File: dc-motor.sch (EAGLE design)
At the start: 80 parts, among them IC1 MEGA32-A, X10 JUMP1-4, X11 JUMP1-4, X3 RIA_3POL, X4 RIA_3POL, X5 RIA_2POL, X6 JUMP1-4, X7 PFVERB10, X8 PFVERB10, X9 JUMP1-4

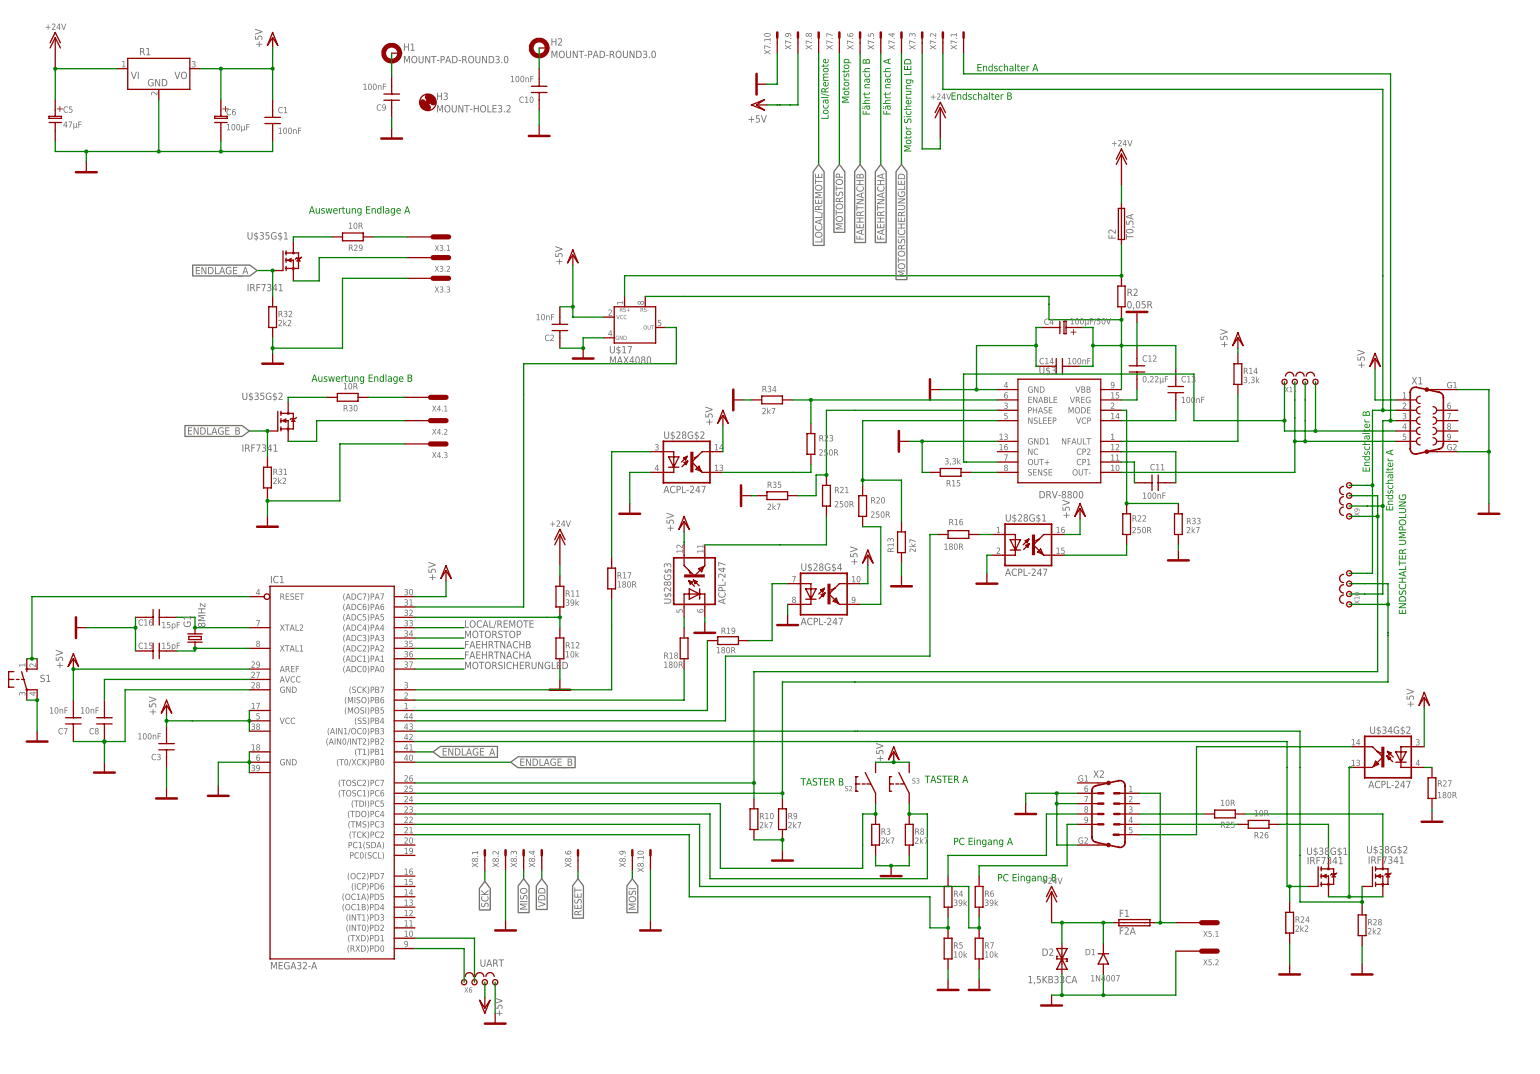
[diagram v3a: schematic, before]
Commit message: ADC wiring changed.
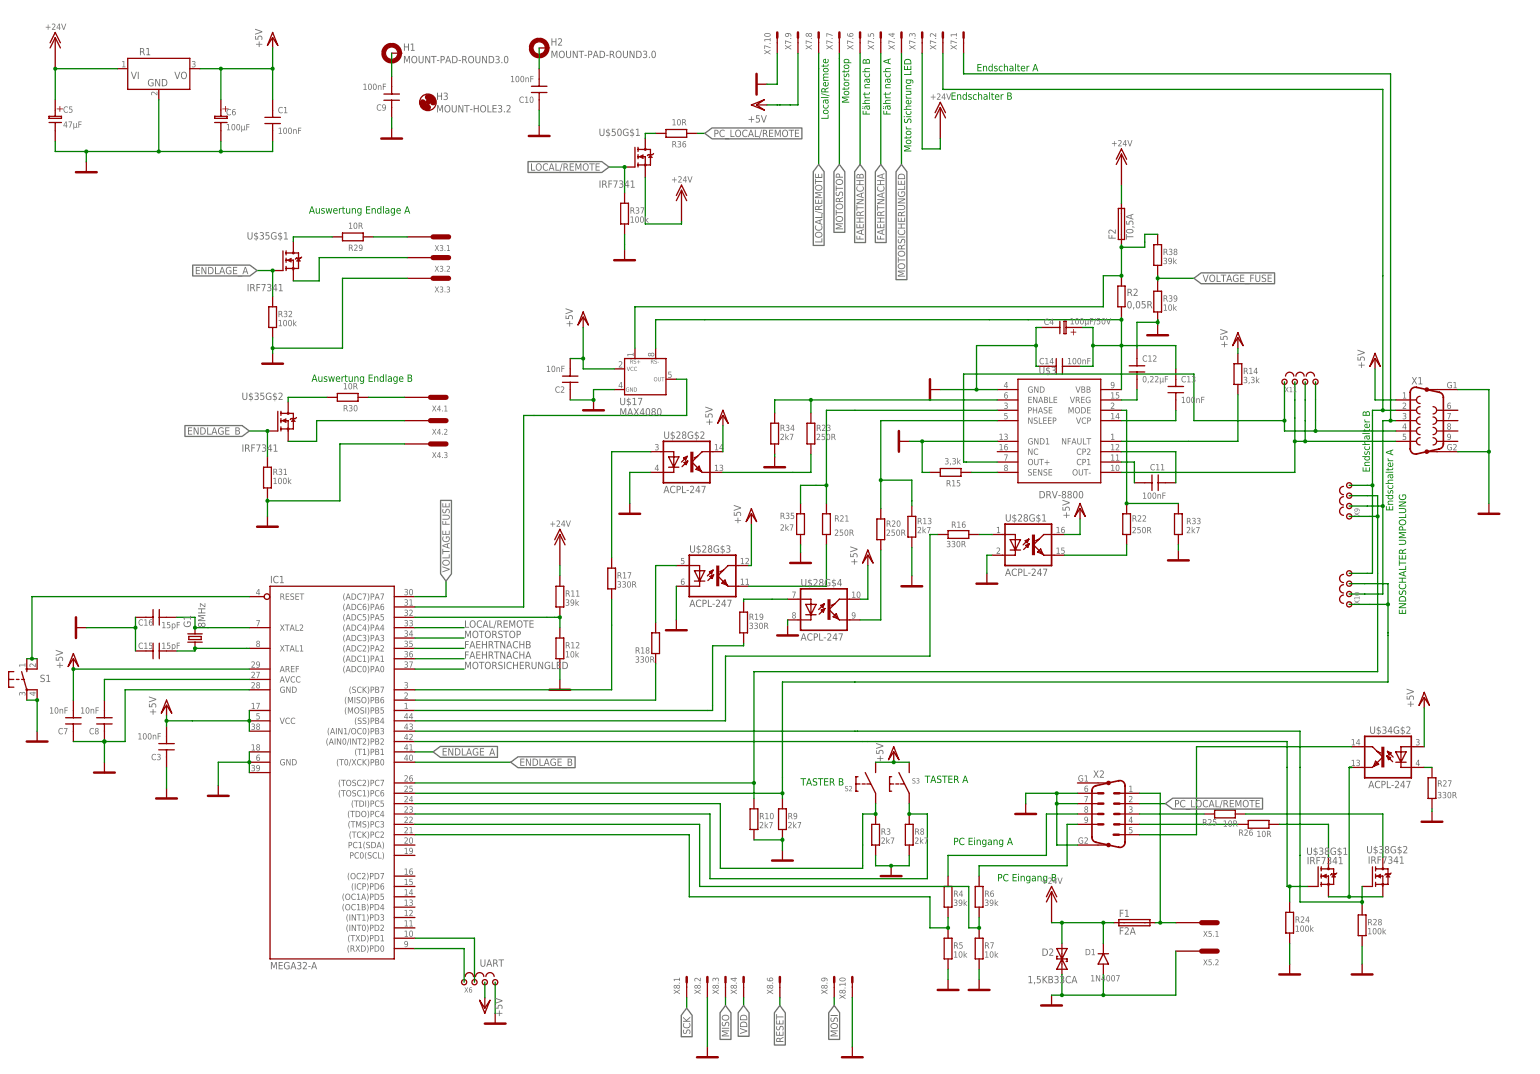
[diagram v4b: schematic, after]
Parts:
- added R36: 10R, Resistor:0805
- added R37: 100k, Resistor:0805
- added R38: 39k, Resistor:0805
- added R39: 10k, Resistor:0805
- added U$50: IRF7341, Transistor:IRF7341
- R16, R17, R18, R19, R27: value 180R -> 330R
- R24, R28, R31, R32: value 2k2 -> 100k
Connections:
- new net N$39: R36.2
- new net PC_LOCAL/REMOTE: R36.1, X2.2
- new net VOLTAGE_FUSE: IC1.(ADC7)PA7, R38.1, R39.2
- net +24V: now also U$50G$1.N-S1
- net GND: now also R37.2, R39.1
- net LOCAL/REMOTE: now also R37.1, U$50G$1.N-G1
- net N$6: now also R38.2
- net VDD: no longer IC1.(ADC7)PA7
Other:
- moved on the sheet: C2, R13, R18, R19, R20, R21, R23, R34, R35, U$17, U$28G$3, U$28G$4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

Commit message: Layout finished
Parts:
- removed X10, X11, X9: JUMP1-4, Connector:JUMP1-4
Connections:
- removed net N$30: U$3.OUT-, X1.5, X11.2, X11.3
- removed net N$5: U$3.OUT+, X1.4, X11.1, X11.4
- new net +24V_LED_µC: IC1.PC1(SDA), X7.3.1
- new net MOTOR: IC1.(INT1)PD3, X1.6
- new net N$41: U$3.OUT+, X1.4
- new net N$44: U$3.OUT-, X1.5
- new net RICHTUNG: IC1.(INT0)PD2, X1.9
- net +24V: no longer X7.3.1
- net GND: now also X1.7, X1.8, X2.G1
- net N$18: no longer X10.1, X10.3
- net N$20: no longer X10.4, X9.4
- net N$22: no longer X10.2, X9.2
- net N$25: no longer X9.1, X9.3
- net N$39: now also U$50G$1.D1
- net N$60: now also IC1.AREF; no longer IC1.AVCC
- net VDD: now also IC1.AVCC; no longer IC1.AREF
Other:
- note removed: "ENDSCHALTER UMPOLUNG"
- moved on the sheet: C7, C8, R36, R37, U$50G$1, X1

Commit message: layout checked
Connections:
- net MOTORSICHERUNGLED renamed FEHLER_LED
- removed net N$20: X1.2, X7.2.1
- removed net N$22: X1.3, X7.1.1
- net N$18: now also X1.3, X7.1.1
- net N$25: now also X1.2, X7.2.1
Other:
- note added: "Fehler_LED"
- note removed: "Motor Sicherung LED"
- moved on the sheet: R24
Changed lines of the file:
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@@
 <setting verticaltext="up"/>
 </settings>
-<grid distance="0.635" unitdist="mm" unit="mm" style="lines" multiple="1" display="yes" altdistance="0.3175" altunitdist="mm" altunit="mm"/>
+<grid distance="0.635" unitdist="mm" unit="mm" style="dots" multiple="1" display="yes" altdistance="0.3175" altunitdist="mm" altunit="mm"/>
 <layers>
 <layer number="1" name="Top" color="4" fill="1" visible="no" active="no"/>
@@
 <text x="220.98" y="259.08" size="1.778" layer="91" font="vector" rot="R270">Fährt nach A</text>
 <text x="215.9" y="259.08" size="1.778" layer="91" font="vector" rot="R270">Fährt nach B</text>
-<text x="226.06" y="259.08" size="1.778" layer="91" font="vector" rot="R270">Motor Sicherung LED</text>
+<text x="226.06" y="259.08" size="1.778" layer="91" font="vector" rot="R270">Fehler_LED</text>
 <text x="340.36" y="144.78" size="1.778" layer="91" font="vector" rot="R90">Endschalter B</text>
 <text x="345.44" y="137.16" size="1.778" layer="91" font="vector" rot="R90">Endschalter A</text>
@@
 </instance>
 <instance part="U$39" gate="G$1" x="338.455" y="34.29" smashed="yes" rot="MR0"/>
-<instance part="U$40" gate="G$1" x="320.675" y="34.29" smashed="yes" rot="MR0"/>
-<instance part="R24" gate="G$1" x="320.675" y="46.99" smashed="yes" rot="R270">
-<attribute name="NAME" x="321.945" y="46.99" size="1.524" layer="95"/>
-<attribute name="VALUE" x="321.945" y="44.7675" size="1.524" layer="96"/>
+<instance part="U$40" gate="G$1" x="320.04" y="34.29" smashed="yes" rot="MR0"/>
+<instance part="R24" gate="G$1" x="320.04" y="46.99" smashed="yes" rot="R270">
+<attribute name="NAME" x="321.31" y="46.99" size="1.524" layer="95"/>
+<attribute name="VALUE" x="321.31" y="44.7675" size="1.524" layer="96"/>
 </instance>
 <instance part="R28" gate="G$1" x="338.455" y="46.355" smashed="yes" rot="R270">
@@
 <pinref part="R24" gate="G$1" pin="2"/>
 <pinref part="U$40" gate="G$1" pin="GND"/>
-<wire x1="320.675" y1="41.91" x2="320.675" y2="36.83" width="0.1524" layer="91"/>
+<wire x1="320.04" y1="41.91" x2="320.04" y2="36.83" width="0.1524" layer="91"/>
 </segment>
 <segment>
@@
 <wire x1="196.215" y1="106.045" x2="213.995" y2="106.045" width="0.1524" layer="91"/>
 <wire x1="213.995" y1="106.045" x2="343.535" y2="106.045" width="0.1524" layer="91"/>
-<wire x1="343.535" y1="106.045" x2="343.535" y2="117.475" width="0.1524" layer="91"/>
-<wire x1="343.535" y1="117.475" x2="343.535" y2="118.745" width="0.1524" layer="91"/>
-<wire x1="343.535" y1="118.745" x2="343.535" y2="125.095" width="0.1524" layer="91"/>
-<wire x1="343.535" y1="125.095" x2="343.535" y2="130.81" width="0.1524" layer="91"/>
-<wire x1="343.535" y1="130.81" x2="343.535" y2="149.225" width="0.1524" layer="91"/>
 <pinref part="IC1" gate="G$1" pin="(TOSC1)PC6"/>
 <wire x1="106.045" y1="78.74" x2="196.215" y2="78.74" width="0.1524" layer="91"/>
 <junction x="196.215" y="78.74"/>
-</segment>
-</net>
-<net name="N$20" class="0">
-<segment>
-<wire x1="340.995" y1="171.45" x2="340.995" y2="157.48" width="0.1524" layer="91"/>
-<wire x1="340.995" y1="172.72" x2="340.995" y2="171.45" width="0.1524" layer="91"/>
+<pinref part="X1" gate="G$1" pin="3"/>
+<wire x1="343.535" y1="170.18" x2="345.44" y2="170.18" width="0.1524" layer="91"/>
+<pinref part="X7" gate=".1" pin="1"/>
+<wire x1="345.44" y1="170.18" x2="346.075" y2="170.18" width="0.1524" layer="91"/>
+<wire x1="240.665" y1="260.35" x2="240.665" y2="255.27" width="0.1524" layer="91"/>
+<wire x1="240.665" y1="255.27" x2="345.44" y2="255.27" width="0.1524" layer="91"/>
+<wire x1="345.44" y1="170.18" x2="345.44" y2="255.27" width="0.1524" layer="91"/>
+<junction x="345.44" y="170.18"/>
+<wire x1="343.535" y1="106.045" x2="343.535" y2="170.18" width="0.1524" layer="91"/>
+</segment>
+</net>
+<net name="N$25" class="0">
+<segment>
+<pinref part="R10" gate="G$1" pin="2"/>
+<wire x1="189.23" y1="108.585" x2="189.23" y2="81.28" width="0.1524" layer="91"/>
+<wire x1="189.23" y1="81.28" x2="189.23" y2="77.47" width="0.1524" layer="91"/>
+<wire x1="189.23" y1="108.585" x2="340.995" y2="108.585" width="0.1524" layer="91"/>
+<wire x1="340.995" y1="108.585" x2="340.995" y2="133.985" width="0.1524" layer="91"/>
+<pinref part="IC1" gate="G$1" pin="(TOSC2)PC7"/>
+<wire x1="106.045" y1="81.28" x2="189.23" y2="81.28" width="0.1524" layer="91"/>
+<junction x="189.23" y="81.28"/>
 <pinref part="X1" gate="G$1" pin="2"/>
 <wire x1="346.075" y1="172.72" x2="343.535" y2="172.72" width="0.1524" layer="91"/>
 <wire x1="343.535" y1="172.72" x2="340.995" y2="172.72" width="0.1524" layer="91"/>
-<wire x1="340.995" y1="154.305" x2="340.995" y2="157.48" width="0.1524" layer="91"/>
 <wire x1="343.535" y1="172.72" x2="343.535" y2="205.74" width="0.1524" layer="91"/>
 <junction x="343.535" y="172.72"/>
@@
 <wire x1="343.535" y1="253.365" x2="235.585" y2="253.365" width="0.1524" layer="91"/>
 <wire x1="235.585" y1="253.365" x2="235.585" y2="260.35" width="0.1524" layer="91"/>
-<wire x1="340.995" y1="154.305" x2="340.995" y2="133.985" width="0.1524" layer="91"/>
-</segment>
-</net>
-<net name="N$25" class="0">
-<segment>
-<pinref part="R10" gate="G$1" pin="2"/>
-<wire x1="189.23" y1="108.585" x2="189.23" y2="81.28" width="0.1524" layer="91"/>
-<wire x1="189.23" y1="81.28" x2="189.23" y2="77.47" width="0.1524" layer="91"/>
-<wire x1="189.23" y1="108.585" x2="340.995" y2="108.585" width="0.1524" layer="91"/>
-<wire x1="340.995" y1="108.585" x2="340.995" y2="131.445" width="0.1524" layer="91"/>
-<wire x1="340.995" y1="131.445" x2="340.995" y2="133.985" width="0.1524" layer="91"/>
-<pinref part="IC1" gate="G$1" pin="(TOSC2)PC7"/>
-<wire x1="106.045" y1="81.28" x2="189.23" y2="81.28" width="0.1524" layer="91"/>
-<junction x="189.23" y="81.28"/>
+<wire x1="340.995" y1="133.985" x2="340.995" y2="172.72" width="0.1524" layer="91"/>
 </segment>
 </net>
@@
 <pinref part="U$38" gate="G$1" pin="N-G1"/>
 <pinref part="R24" gate="G$1" pin="1"/>
-<wire x1="325.12" y1="55.88" x2="320.675" y2="55.88" width="0.1524" layer="91"/>
-<wire x1="320.675" y1="55.88" x2="320.675" y2="52.07" width="0.1524" layer="91"/>
-<wire x1="320.04" y1="55.88" x2="320.675" y2="55.88" width="0.1524" layer="91"/>
-<junction x="320.675" y="55.88"/>
+<wire x1="325.12" y1="55.88" x2="320.04" y2="55.88" width="0.1524" layer="91"/>
+<wire x1="320.04" y1="55.88" x2="320.04" y2="52.07" width="0.1524" layer="91"/>
+<junction x="320.04" y="55.88"/>
 </segment>
 </net>
@@
 </segment>
 </net>
-<net name="MOTORSICHERUNGLED" class="0">
+<net name="FEHLER_LED" class="0">
 <segment>
 <pinref part="X7" gate=".4" pin="1"/>
@@
 </segment>
 </net>
-<net name="N$22" class="0">
-<segment>
-<pinref part="X1" gate="G$1" pin="3"/>
-<wire x1="343.535" y1="149.225" x2="343.535" y2="170.18" width="0.1524" layer="91"/>
-<wire x1="343.535" y1="170.18" x2="345.44" y2="170.18" width="0.1524" layer="91"/>
-<pinref part="X7" gate=".1" pin="1"/>
-<wire x1="345.44" y1="170.18" x2="346.075" y2="170.18" width="0.1524" layer="91"/>
-<wire x1="240.665" y1="260.35" x2="240.665" y2="255.27" width="0.1524" layer="91"/>
-<wire x1="240.665" y1="255.27" x2="345.44" y2="255.27" width="0.1524" layer="91"/>
-<wire x1="345.44" y1="170.18" x2="345.44" y2="255.27" width="0.1524" layer="91"/>
-<junction x="345.44" y="170.18"/>
-</segment>
-</net>

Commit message: Layout fixed
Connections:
- removed net N$33: R14.1, U$3.NFAULT
- new net NFAULT: IC1.PC0(SCL), R14.1, U$3.NFAULT
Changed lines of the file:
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@@
 </segment>
 </net>
-<net name="N$33" class="0">
+<net name="NFAULT" class="0">
 <segment>
 <pinref part="U$3" gate="G$1" pin="NFAULT"/>
@@
 <pinref part="R14" gate="G$1" pin="1"/>
 <wire x1="307.975" y1="165.1" x2="307.975" y2="176.53" width="0.1524" layer="91"/>
+<wire x1="307.975" y1="176.53" x2="311.785" y2="176.53" width="0.1524" layer="91"/>
+<junction x="307.975" y="176.53"/>
+<label x="311.785" y="176.53" size="1.778" layer="95" font="vector" xref="yes"/>
+</segment>
+<segment>
+<pinref part="IC1" gate="G$1" pin="PC0(SCL)"/>
+<wire x1="106.045" y1="63.5" x2="132.08" y2="63.5" width="0.1524" layer="91"/>
+<label x="132.08" y="63.5" size="1.778" layer="95" font="vector" xref="yes"/>
 </segment>
 </net>

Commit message: Layout edited
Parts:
- removed X7: PFVERB10, Connector:PFVERB10
- added SV1: (no value), con-lstb:MA06-2
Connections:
- removed net FEHLER_LED: IC1.(ADC0)PA0, X7.4.1
- removed net N$18: IC1.(TOSC1)PC6, R9.2, X1.3, X7.1.1
- removed net N$25: IC1.(TOSC2)PC7, R10.2, X1.2, X7.2.1
- new net ENDSCHALTER_A: IC1.(TOSC1)PC6, R9.2, SV1.3, X1.3
- new net ENDSCHALTER_B: IC1.(TOSC2)PC7, R10.2, SV1.7, X1.2
- new net RGB_BLAU: IC1.(ICP)PD6, SV1.6
- new net RGB_GRUEN: IC1.(OC1A)PD5, SV1.2
- new net RGB_ROT: IC1.(OC2)PD7, SV1.4
- net +24V_LED_µC: now also SV1.8; no longer IC1.PC1(SDA), X7.3.1
- net FAEHRTNACHA: now also SV1.1; no longer X7.5.1
- net FAEHRTNACHB: now also SV1.5; no longer X7.6.1
- net GND: now also SV1.11; no longer X7.10.1
- net LOCAL/REMOTE: now also SV1.10; no longer X7.8.1
- net MOTORSTOP: now also SV1.9; no longer X7.7.1
- net NFAULT: now also IC1.PC1(SDA); no longer IC1.PC0(SCL)
- net VDD: now also SV1.12; no longer X7.9.1
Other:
- note removed: "Fehler_LED"
- note removed: "Fährt nach A"
- note removed: "Fährt nach B"
- note removed: "Local/Remote"
- note removed: "Motorstop"
